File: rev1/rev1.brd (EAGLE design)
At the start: 100 x 80 mm, 26 parts, among them IC1 ATMEGA168-AU, Q1 MOSFET-NCHANNEL-IRLR3705ZPBF, Y1 16MHz

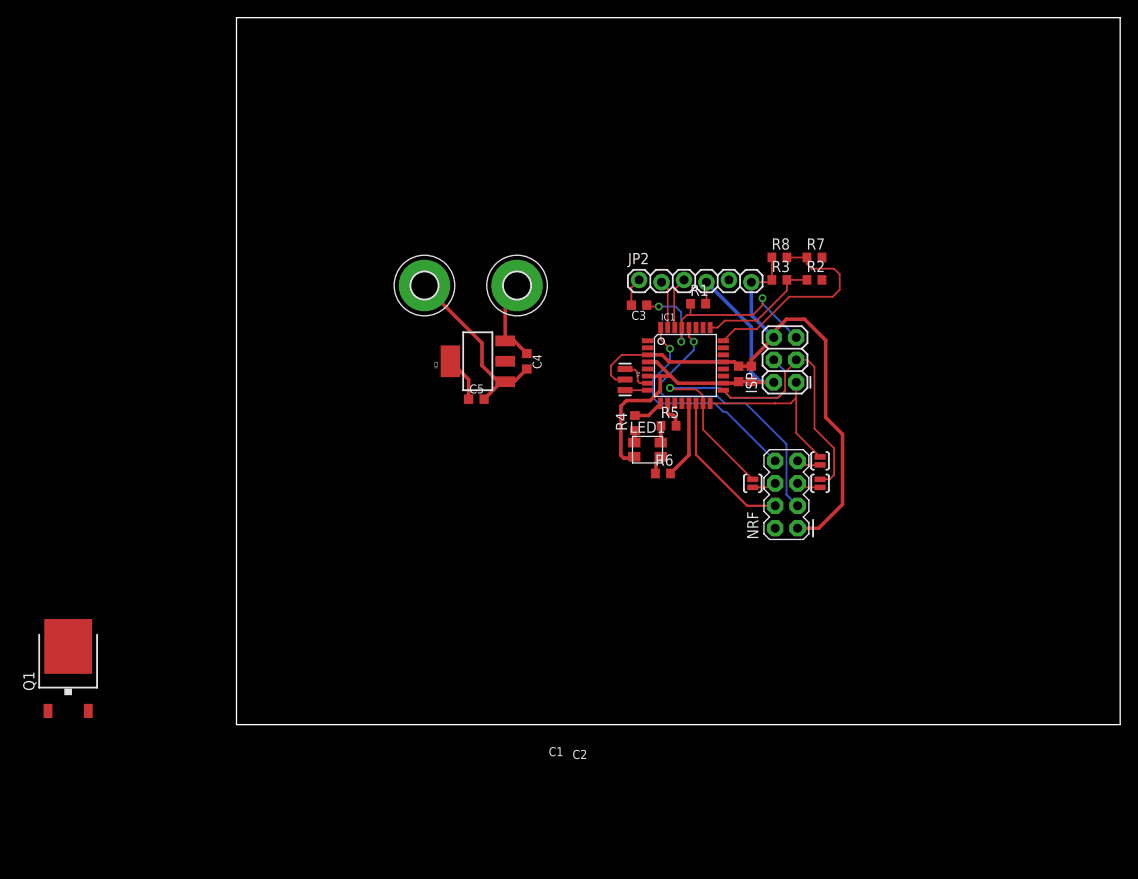
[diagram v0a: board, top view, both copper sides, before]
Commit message: Added charge pump for v-gate
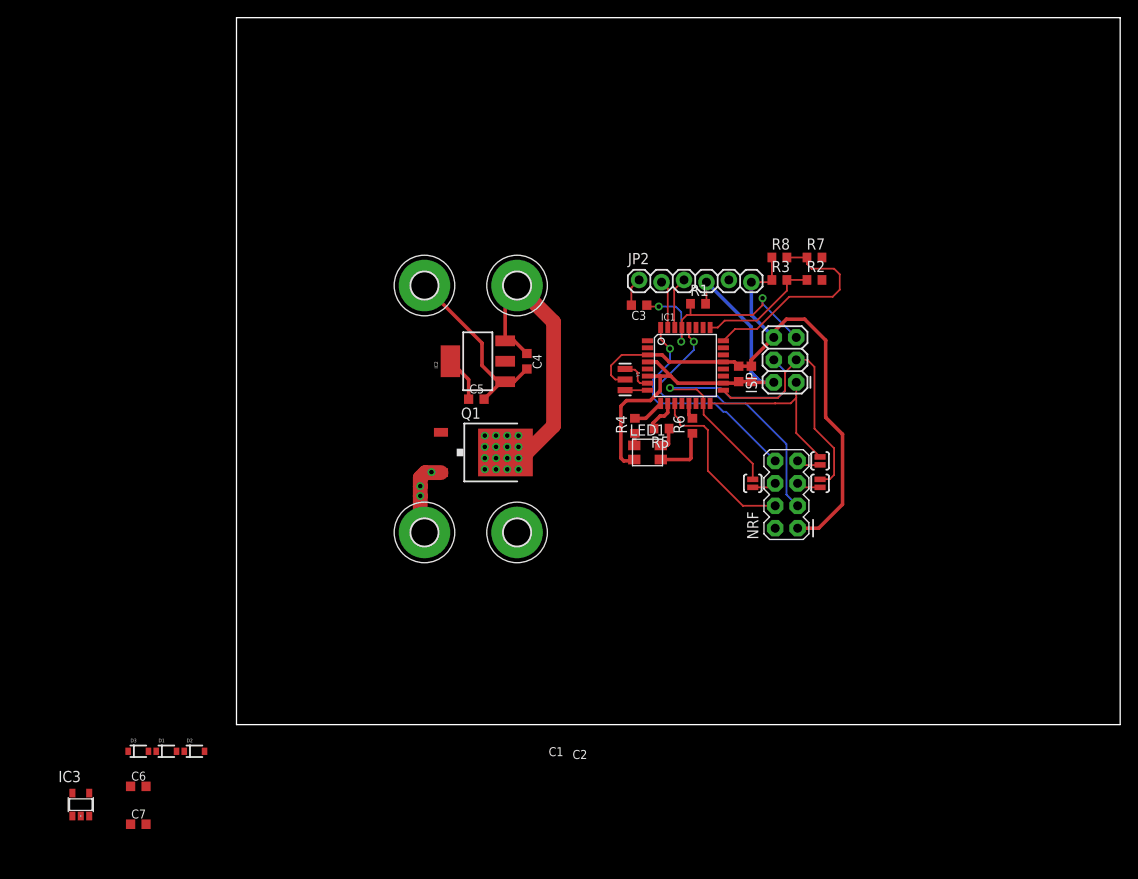
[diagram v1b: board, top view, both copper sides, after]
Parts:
- added C6: 47nF, resistor:C0603K
- added C7: 0.1uF, resistor:C0603K
- added D1, D2, D3: (no value), SparkFun-DiscreteSemi:SOD-323
- added H3, H4: MOUNT-PAD-ROUND3.0, holes:3,0-PAD
- added IC3: 74AHC1G04DBV, 74xx-little-de:SOT23-5
- moved Q1 53.5 mm to (29.2, 30.8), turned to 270 degrees
- moved R6 6.34 mm to (51.6, 33.8), turned to 90 degrees
- moved R5 0.85 mm to (48.1, 33.5), turned to 180 degrees
- moved R4 0.32 mm to (45.1, 33.8)
- moved LED1 0.32 mm to (46.5, 30.8)
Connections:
- new net FET-PUMP: Q1.1
- new net N$10: C6.2, D1.2, D3.1
- new net N$8: C7.2, D1.1, D2.2
- new net PUMPA: C6.1, IC1.14, IC3.2
- new net PUMPB: C7.1, IC3.4
- new net V+: D2.1
- net +15V: now also D3.2, H3.B3,0, Q1.2
- net +18V: now also Q1.TAB
- net +5V: now also IC3.5
- net CSN: now also IC1.11; no longer IC1.14
- net FET-DRIVE: no longer Q1.1
- net GND: now also H4.B3,0, IC3.3
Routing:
- net +18V: track 10.1 -> 34.3 mm
- net +15V: track 0.00 -> 8.97 mm, vias 0 -> 2
- net N$9: track 8.80 -> 1.85 mm
- net N$6: track 2.15 -> 6.36 mm
- net CSN: track 17.2 -> 19.9 mm
- net N$4: track 1.91 -> 2.71 mm
- net N$7: track 3.20 -> 3.86 mm

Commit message: Schematic pre-finished. Needs values added
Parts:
- added C8: 1uF, resistor:C0603K
- added Q2: MOSFET-PCHANNELSMD, SparkFun-DiscreteSemi:SOT23-3
- added Q3: MOSFET-NCHANNELBSS138, SparkFun-DiscreteSemi:SOT23
- added R9: 10k, resistor:R0603
- C7: value 0.1uF -> 47nF
- D1, D2, D3: value (none) -> DIODE-SCHOTTKY; device SparkFun-DiscreteSemi:SOD-323 -> SparkFun-DiscreteSemi:SOD-523
- moved IC3 60.0 mm to (17.6, 39.5), turned to 270 degrees
- moved C7 58.5 mm to (21.0, 37.6), turned to 270 degrees
- moved C6 55.8 mm to (22.4, 37.6), turned to 270 degrees
- moved D3 44.7 mm to (18.1, 30.8)
- moved D1 44.5 mm to (18.1, 33.0), turned to 180 degrees
- moved D2 44.4 mm to (18.1, 35.1)
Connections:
- new net N$28: Q2.3, Q3.3
- net +15V: now also D3.A, R9.1; no longer D3.2
- net FET-DRIVE: now also Q2.1, Q3.1
- net FET-PUMP: now also R9.2
- net GND: now also C8.1, Q3.2
- net N$10: now also D1.A, D3.C; no longer D1.2, D3.1
- net N$8: now also D1.C, D2.A; no longer D1.1, D2.2
- net V+: now also C8.2, D2.C, Q2.2; no longer D2.1
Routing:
- net N$10: track 0.00 -> 13.0 mm
- net PUMPA: track 0.00 -> 6.71 mm
- net N$8: track 0.00 -> 6.63 mm
- net +15V: track 8.97 -> 14.3 mm
- net V+: track 0.00 -> 2.96 mm
- net PUMPB: track 0.00 -> 2.07 mm
- net GND: track 91.4 -> 93.3 mm
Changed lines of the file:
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@@
 <element name="H3" library="holes" package="3,0-PAD" value="MOUNT-PAD-ROUND3.0" x="21.2725" y="21.74875" rot="R90"/>
 <element name="H4" library="holes" package="3,0-PAD" value="MOUNT-PAD-ROUND3.0" x="31.75" y="21.74875" rot="R90"/>
-<element name="D2" library="SparkFun-DiscreteSemi" package="SOD-323" value="" x="-4.7625" y="-3.01625"/>
-<element name="D1" library="SparkFun-DiscreteSemi" package="SOD-323" value="" x="-7.9375" y="-3.01625"/>
-<element name="D3" library="SparkFun-DiscreteSemi" package="SOD-323" value="" x="-11.1125" y="-3.01625"/>
-<element name="C6" library="resistor" package="C0603K" value="47nF" x="-11.1125" y="-6.985"/>
-<element name="C7" library="resistor" package="C0603K" value="0.1uF" x="-11.1125" y="-11.27125"/>
-<element name="IC3" library="74xx-little-de" package="SOT23-5" value="74AHC1G04DBV" x="-17.62125" y="-9.04875"/>
+<element name="D2" library="SparkFun-DiscreteSemi" package="SOD-523" value="DIODE-SCHOTTKY" x="18.0975" y="35.08375"/>
+<element name="D1" library="SparkFun-DiscreteSemi" package="SOD-523" value="DIODE-SCHOTTKY" x="18.0975" y="33.02" rot="R180"/>
+<element name="D3" library="SparkFun-DiscreteSemi" package="SOD-523" value="DIODE-SCHOTTKY" x="18.0975" y="30.7975"/>
+<element name="C6" library="resistor" package="C0603K" value="47nF" x="22.38375" y="37.62375" rot="R270"/>
+<element name="C7" library="resistor" package="C0603K" value="47nF" x="20.955" y="37.62375" rot="R270"/>
+<element name="IC3" library="74xx-little-de" package="SOT23-5" value="74AHC1G04DBV" x="17.62125" y="39.52875" rot="R270"/>
+<element name="C8" library="resistor" package="C0603K" value="1uF" x="15.71625" y="36.03625" rot="R270"/>
+<element name="R9" library="resistor" package="R0603" value="10k" x="1.5875" y="-7.62"/>
+<element name="Q3" library="SparkFun-DiscreteSemi" package="SOT23" value="MOSFET-NCHANNELBSS138" x="-1.5875" y="-13.6525">
+<attribute name="PROD_ID" value="TRANS-00830" x="-1.5875" y="-13.6525" size="1.778" layer="27" display="off"/>
+</element>
+<element name="Q2" library="SparkFun-DiscreteSemi" package="SOT23-3" value="MOSFET-PCHANNELSMD" x="-4.7625" y="-13.97"/>
 </elements>
 <signals>
@@
 <wire x1="30.4038" y1="41.11625" x2="43.4975" y2="36.03625" width="0" layer="19" extent="1-1"/>
 <wire x1="26.27125" y1="39.051" x2="30.4038" y2="41.11625" width="0" layer="19" extent="1-1"/>
-<wire x1="-18.57125" y1="-7.74875" x2="26.27125" y2="36.83" width="0" layer="19" extent="1-1"/>
+<wire x1="18.92125" y1="40.47875" x2="24.206" y2="41.11625" width="0" layer="19" extent="1-1"/>
 </signal>
 <signal name="SCK">
@@
 <contactref element="H4" pad="B3,0"/>
 <contactref element="IC3" pad="3"/>
+<contactref element="C8" pad="1"/>
+<wire x1="15.71625" y1="36.91125" x2="16.33125" y2="37.52625" width="0.2032" layer="1"/>
+<wire x1="16.33125" y1="37.52625" x2="16.33125" y2="38.57875" width="0.2032" layer="1"/>
+<contactref element="Q3" pad="2"/>
 <wire x1="46.5074" y1="41.84" x2="46.5074" y2="40.24" width="0" layer="19" extent="1-1"/>
 <wire x1="32.86125" y1="40.24125" x2="42.38625" y2="40.64" width="0" layer="19" extent="1-1"/>
+<wire x1="16.33125" y1="38.57875" x2="27.78125" y2="40.64" width="0" layer="19" extent="1-1"/>
 <wire x1="31.75" y1="21.74875" x2="28.02125" y2="36.83" width="0" layer="19" extent="1-1"/>
-<wire x1="-16.67125" y1="-10.33875" x2="31.75" y2="21.74875" width="0" layer="19" extent="1-1"/>
+<wire x1="-0.6375" y1="-14.7525" x2="31.75" y2="21.74875" width="0" layer="19" extent="1-1"/>
 </signal>
 <signal name="VBAT-READ">
@@
 <contactref element="H3" pad="B3,0"/>
 <wire x1="23.14" y1="28.5175" x2="21.37375" y2="28.5175" width="1.6764" layer="1"/>
-<wire x1="21.37375" y1="28.5175" x2="20.79625" y2="27.94" width="1.6764" layer="1"/>
+<wire x1="21.37375" y1="28.5175" x2="21.034375" y2="28.178125" width="1.6764" layer="1"/>
+<wire x1="21.034375" y1="28.178125" x2="20.79625" y2="27.94" width="1.6764" layer="1"/>
 <wire x1="20.79625" y1="27.94" x2="20.79625" y2="26.9875" width="1.6764" layer="1"/>
 <wire x1="20.79625" y1="26.9875" x2="20.79625" y2="25.87625" width="1.6764" layer="1"/>
@@
 <via x="20.79625" y="26.9875" extent="1-16" drill="0.508"/>
 <via x="20.79625" y="25.87625" extent="1-16" drill="0.508"/>
-<contactref element="D3" pad="2"/>
+<contactref element="D3" pad="A"/>
+<wire x1="21.034375" y1="29.486875" x2="21.034375" y2="28.178125" width="0.2032" layer="1"/>
+<wire x1="17.5475" y1="30.7975" x2="19.72375" y2="30.7975" width="0.2032" layer="1"/>
+<wire x1="19.72375" y1="30.7975" x2="21.034375" y2="29.486875" width="0.2032" layer="1"/>
+<contactref element="R9" pad="1"/>
 <wire x1="23.14" y1="28.5175" x2="66.255" y2="50.32375" width="0" layer="19" extent="1-1"/>
-<wire x1="-9.9625" y1="-3.01625" x2="20.79625" y2="22.225" width="0" layer="19" extent="1-1"/>
+<wire x1="0.7375" y1="-7.62" x2="21.2725" y2="21.74875" width="0" layer="19" extent="1-1"/>
 </signal>
 <signal name="FET-DRIVE">
 <contactref element="IC1" pad="1"/>
+<contactref element="Q2" pad="1"/>
+<contactref element="Q3" pad="1"/>
+<wire x1="-2.5375" y1="-14.7525" x2="46.5074" y2="43.44" width="0" layer="19" extent="1-1"/>
+<wire x1="-5.7125" y1="-14.97" x2="-2.5375" y2="-14.7525" width="0" layer="19" extent="1-1"/>
 </signal>
 <signal name="N$1">
@@
 <signal name="FET-PUMP">
 <contactref element="Q1" pad="1"/>
+<contactref element="R9" pad="2"/>
+<wire x1="2.4375" y1="-7.62" x2="23.14" y2="33.0775" width="0" layer="19" extent="1-1"/>
 </signal>
 <signal name="N$11">
@@
 </signal>
 <signal name="N$8">
-<contactref element="D2" pad="2"/>
-<contactref element="D1" pad="1"/>
+<contactref element="D2" pad="A"/>
+<contactref element="D1" pad="C"/>
 <contactref element="C7" pad="2"/>
-<wire x1="-9.0875" y1="-3.01625" x2="-10.2375" y2="-11.27125" width="0" layer="19" extent="1-1"/>
-<wire x1="-3.6125" y1="-3.01625" x2="-9.0875" y2="-3.01625" width="0" layer="19" extent="1-1"/>
+<wire x1="17.5475" y1="33.02" x2="17.5475" y2="35.08375" width="0.2032" layer="1"/>
+<wire x1="20.08375" y1="35.08375" x2="17.5475" y2="35.08375" width="0.2032" layer="1"/>
+<wire x1="20.08375" y1="35.08375" x2="20.955" y2="35.955" width="0.2032" layer="1"/>
+<wire x1="20.955" y1="35.955" x2="20.955" y2="36.74875" width="0.2032" layer="1"/>
 </signal>
 <signal name="N$10">
-<contactref element="D3" pad="1"/>
-<contactref element="D1" pad="2"/>
+<contactref element="D3" pad="C"/>
+<contactref element="D1" pad="A"/>
 <contactref element="C6" pad="2"/>
-<wire x1="-12.2625" y1="-3.01625" x2="-10.2375" y2="-6.985" width="0" layer="19" extent="1-1"/>
-<wire x1="-6.7875" y1="-3.01625" x2="-10.2375" y2="-6.985" width="0" layer="19" extent="1-1"/>
+<wire x1="18.6475" y1="30.7975" x2="16.9475" y2="31.90875" width="0.2032" layer="1"/>
+<wire x1="16.9475" y1="31.90875" x2="18.6475" y2="33.02" width="0.2032" layer="1"/>
+<wire x1="22.38375" y1="36.74875" x2="22.38375" y2="36.03625" width="0.2032" layer="1"/>
+<wire x1="20.32" y1="33.9725" x2="20.32" y2="32.0675" width="0.2032" layer="1"/>
+<wire x1="20.32" y1="32.0675" x2="20.16125" y2="31.90875" width="0.2032" layer="1"/>
+<wire x1="20.16125" y1="31.90875" x2="16.9475" y2="31.90875" width="0.2032" layer="1"/>
+<wire x1="22.38375" y1="36.03625" x2="20.32" y2="33.9725" width="0.2032" layer="1"/>
 </signal>
 <signal name="PUMPA">
@@
 <contactref element="IC3" pad="2"/>
 <contactref element="IC1" pad="14"/>
-<wire x1="-11.9875" y1="-6.985" x2="52" y2="36.3474" width="0" layer="19" extent="1-1"/>
-<wire x1="-17.62125" y1="-10.33875" x2="-11.9875" y2="-6.985" width="0" layer="19" extent="1-1"/>
+<wire x1="16.33125" y1="39.52875" x2="21.74875" y2="39.52875" width="0.2032" layer="1"/>
+<wire x1="21.74875" y1="39.52875" x2="22.38375" y2="38.89375" width="0.2032" layer="1"/>
+<wire x1="22.38375" y1="38.89375" x2="22.38375" y2="38.49875" width="0.2032" layer="1"/>
+<wire x1="22.38375" y1="38.49875" x2="52" y2="36.3474" width="0" layer="19" extent="1-1"/>
 </signal>
 <signal name="PUMPB">
 <contactref element="C7" pad="1"/>
 <contactref element="IC3" pad="4"/>
-<wire x1="-11.9875" y1="-11.27125" x2="-16.67125" y2="-7.74875" width="0" layer="19" extent="1-1"/>
+<wire x1="18.92125" y1="38.57875" x2="19.00125" y2="38.49875" width="0.2032" layer="1"/>
+<wire x1="19.00125" y1="38.49875" x2="20.955" y2="38.49875" width="0.2032" layer="1"/>
 </signal>
 <signal name="V+">
-<contactref element="D2" pad="1"/>
+<contactref element="D2" pad="C"/>
+<contactref element="C8" pad="2"/>
+<wire x1="15.71625" y1="35.16125" x2="15.79375" y2="35.08375" width="0.2032" layer="1"/>
+<wire x1="15.79375" y1="35.08375" x2="18.6475" y2="35.08375" width="0.2032" layer="1"/>
+<contactref element="Q2" pad="2"/>
+<wire x1="-3.8125" y1="-14.97" x2="15.79375" y2="35.08375" width="0" layer="19" extent="1-1"/>
+</signal>
+<signal name="N$28">
+<contactref element="Q3" pad="3"/>
+<contactref element="Q2" pad="3"/>
+<wire x1="-1.5875" y1="-12.5525" x2="-4.7625" y2="-12.87" width="0" layer="19" extent="1-1"/>
 </signal>
 </signals>

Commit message: Board laid out
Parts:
- IC2: value (none) -> 5v
- Q2: value MOSFET-PCHANNELSMD -> MOSFET-PCHANNEL; device SparkFun-DiscreteSemi:SOT23-3 -> SparkFun-DiscreteSemi:SOT23
- moved Q2 93.1 mm to (74.3, 35.2), turned to 270 degrees
- moved Q3 92.4 mm to (74.3, 39.1), turned to 270 degrees
- moved R9 84.4 mm to (76.0, 32.1), turned to 90 degrees
- moved H2 71.3 mm to (92.4, 54.6)
- moved C5 64.9 mm to (86.5, 63.0)
- moved IC2 64.8 mm to (86.5, 67.5)
- moved C4 64.7 mm to (91.9, 67.5)
- moved C8 62.0 mm to (76.4, 23.0), turned to 90 degrees
- moved H3 60.8 mm to (81.9, 26.7)
- moved H4 60.8 mm to (92.4, 26.7)
- moved D3 57.3 mm to (74.9, 23.3), turned to 90 degrees
- moved D1 57.3 mm to (74.9, 25.9), turned to 90 degrees
- moved D2 57.2 mm to (74.9, 28.4), turned to 90 degrees
- moved IC3 56.7 mm to (71.4, 21.7), turned to 90 degrees
- moved Q1 53.0 mm to (81.6, 39.1), turned to 0 degrees
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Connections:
- removed net N$28: Q2.3, Q3.3
- net FET-PUMP: now also Q2.3, Q3.3
- net VBAT-READ: now also IC1.24; no longer IC1.25
- net VIN-READ: now also IC1.25; no longer IC1.24
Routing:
- net +5V: track 55.4 -> 134.3 mm
- net GND: track 93.3 -> 149.3 mm
- net VBAT-READ: track 13.9 -> 62.2 mm, vias 0 -> 2
- net FET-DRIVE: track 0.00 -> 47.4 mm
- net PUMPA: track 6.71 -> 39.5 mm
- net +15V: track 14.3 -> 34.7 mm, vias 2 -> 7
- net VIN-READ: track 24.5 -> 42.0 mm
- net FET-PUMP: track 0.00 -> 9.71 mm
- net V+: track 2.96 -> 12.0 mm
- net N$10: track 13.0 -> 5.05 mm
- net PUMPB: track 2.07 -> 6.59 mm
- net +18V: track 34.3 -> 30.0 mm, vias 0 -> 17
- net RST: track 28.0 -> 23.9 mm
- net N$8: track 6.63 -> 4.13 mm
- net N$9: track 1.85 -> 2.64 mm
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- added copper zone on layer 1, net +15V
- added copper zone on layer 16, net +15V
- added copper zone on layer 1, net +18V
- added copper zone on layer 16, net +18V
- added copper zone on layer 1, net GND
- added copper zone on layer 16, net GND
